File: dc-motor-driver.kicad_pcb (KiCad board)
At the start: 2 copper layers, 19.6 x 31.9 mm, 18 parts, among them J1 BAT, J2 Logic, J3 FL, J4 RL, J5 FR, J6 RR, J7 Power, Q1 IRF7303, Q2 IRF7303

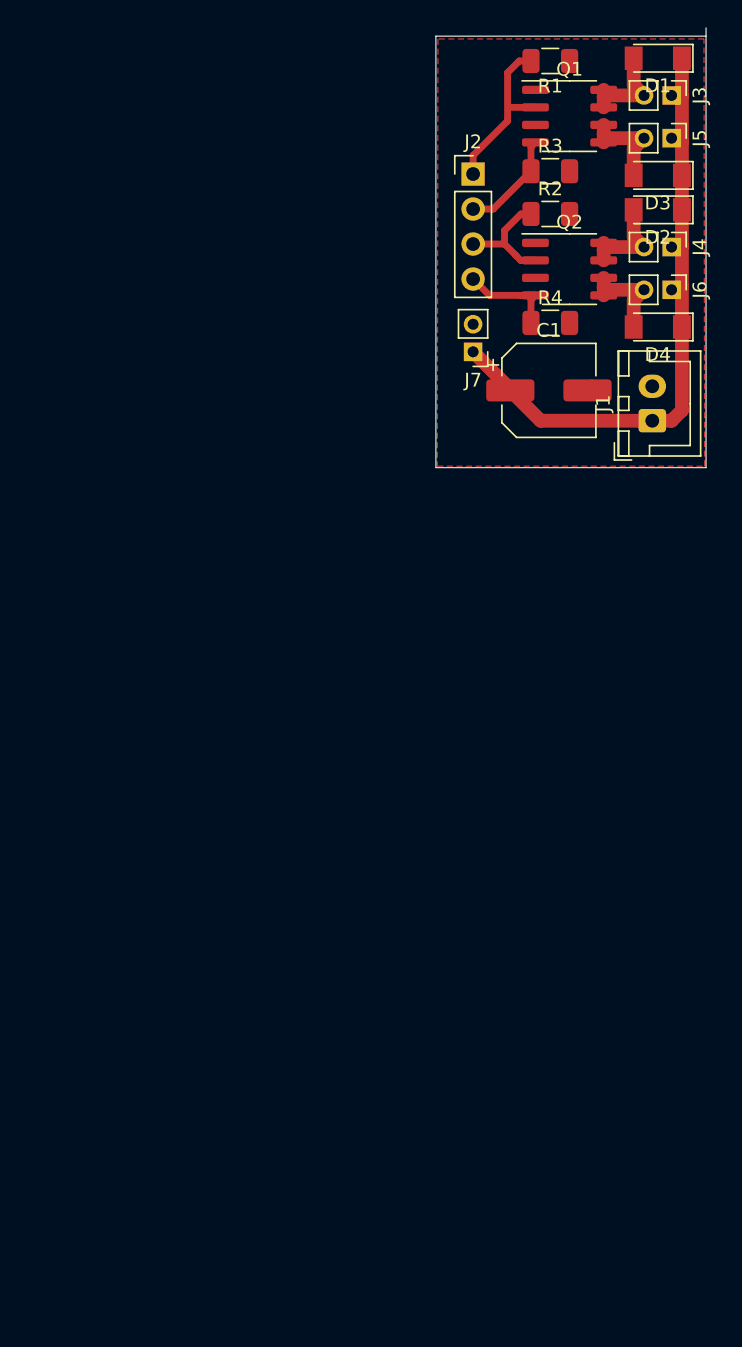
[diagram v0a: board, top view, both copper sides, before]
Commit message: Redesigned the board to work with TTGO T7 modules.
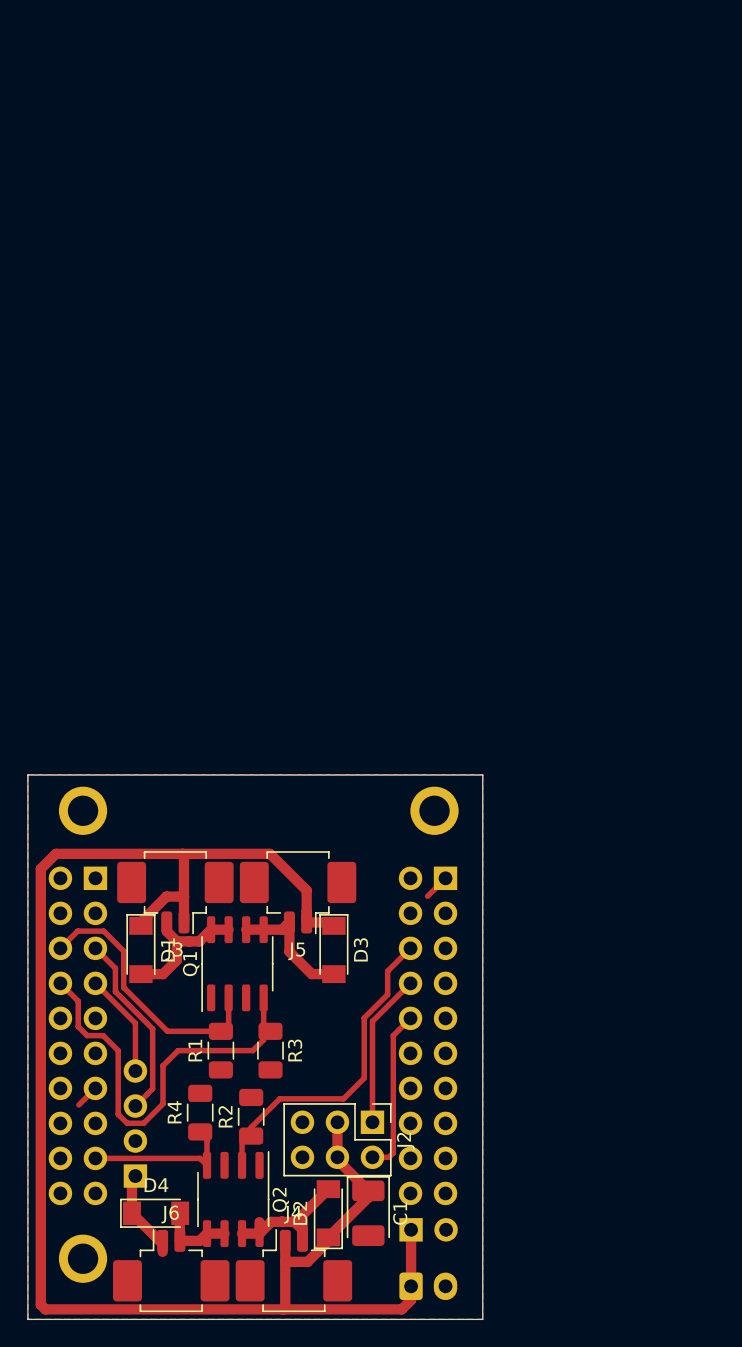
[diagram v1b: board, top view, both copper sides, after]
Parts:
- added ?: MountingHole_2.2mm_M2, MountingHole:MountingHole_2.2mm_M2, F.Cu at (83.0, 112.6)
- added ?: MountingHole_2.2mm_M2, MountingHole:MountingHole_2.2mm_M2, F.Cu at (83.0, 145.1)
- added ?: MountingHole_2.2mm_M2, MountingHole:MountingHole_2.2mm_M2, F.Cu at (108.5, 112.6)
- added J10: Right, Connector_PinHeader_2.54mm:PinHeader_2x10_P2.54mm_Vertical, B.Cu at (83.9, 117.5)
- added J8: MPU, Connector_PinHeader_2.54mm:PinHeader_1x04_P2.54mm_Vertical, B.Cu at (86.8, 139.1)
- added J9: Left, Connector_PinHeader_2.54mm:PinHeader_2x10_P2.54mm_Vertical, B.Cu at (109.3, 117.5)
- C1: value 2000uF -> C; footprint Capacitor_SMD:CP_Elec_6.3x5.9 -> Capacitor_Tantalum_SMD:CP_EIA-3528-21_Kemet-B_Pad1.50x2.35mm_HandSolder
- J1: moved to B.Cu
- J2: value Logic -> Conn_02x03_Odd_Even; footprint Connector_PinHeader_2.54mm:PinHeader_1x04_P2.54mm_Vertical -> Connector_PinHeader_2.54mm:PinHeader_2x03_P2.54mm_Vertical
- J3, J4, J5, J6: footprint Connector_PinHeader_2.00mm:PinHeader_1x02_P2.00mm_Vertical -> Connector_Molex:Molex_PicoBlade_53261-0271_1x02-1MP_P1.25mm_Horizontal
- J7: footprint Connector_PinHeader_2.00mm:PinHeader_1x02_P2.00mm_Vertical -> Connector_PinHeader_2.54mm:PinHeader_1x02_P2.54mm_Vertical; moved to B.Cu
- moved J6 80.1 mm to (89.4, 146.2), turned to 0 degrees
- moved J4 79.4 mm to (98.3, 146.2), turned to 0 degrees
- moved D2 76.6 mm to (100.8, 141.8), turned to 90 degrees
- moved R1 75.7 mm to (93.0, 130.0), turned to 90 degrees
- moved D1 74.8 mm to (87.2, 122.7), turned to 270 degrees
- moved D4 73.9 mm to (88.3, 141.8), turned to 0 degrees
- moved Q2 71.8 mm to (93.9, 140.8), turned to 270 degrees
- moved J2 69.2 mm to (104.0, 135.2), turned to 270 degrees
- moved R2 69.0 mm to (95.2, 134.8), turned to 90 degrees
- moved J3 67.9 mm to (89.7, 118.3), turned to 180 degrees
- moved R3 67.0 mm to (96.6, 130.0), turned to 270 degrees
- moved Q1 66.1 mm to (94.2, 123.7), turned to 90 degrees
- moved J1 65.2 mm to (106.8, 147.1), turned to 0 degrees
- moved J7 63.9 mm to (106.8, 143.0), turned to 270 degrees
- moved R4 62.7 mm to (91.5, 134.5), turned to 90 degrees
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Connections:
- J2 pad 1: /FL -> /ServoA
- J2 pad 2: /FR -> /ServoB
- J2 pad 3: /RL -> VCC
- J2 pad 4: /RR -> VCC
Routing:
- net VCC: track 46.4 -> 124.5 mm
- net /FR: track 8.02 -> 29.9 mm
- net /RL: track 8.42 -> 23.5 mm
- net /SCL: track 0.00 -> 13.7 mm
- net /ServoB: track 0.00 -> 12.6 mm
- net /ServoA: track 0.00 -> 11.2 mm
- net /FL: track 12.6 -> 20.7 mm
- net /SDA: track 0.00 -> 7.56 mm
- net /RR: track 8.22 -> 12.2 mm
- net Net-(D2-Pad2): track 7.30 -> 11.2 mm
- net GND: track 0.42 -> 3.54 mm
- net Net-(D1-Pad2): track 7.26 -> 10.2 mm
- net Net-(D3-Pad2): track 7.32 -> 9.84 mm
- net Net-(D4-Pad2): track 7.28 -> 5.68 mm
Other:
- board size 19.6 x 31.9 mm -> 33 x 39.5 mm

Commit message: Added a third servo and an LED.
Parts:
- removed the D4 at (88.3, 141.8)
- removed the J2 at (104.0, 135.2)
- removed the J3 at (89.7, 118.3)
- removed the J9 at (109.3, 117.5)
- added C1: 20uF, Capacitor_SMD:C_1206_3216Metric_Pad1.42x1.75mm_HandSolder, F.Cu at (89.2, 137.9)
- added D2: LL4148, Diode_SMD:D_MiniMELF, F.Cu at (98.5, 124.4)
- added D5: LL4148, Diode_SMD:D_MiniMELF, F.Cu at (88.3, 141.8)
- added J1: Conn_01x03, Connector_PinHeader_2.54mm:PinHeader_1x03_P2.54mm_Vertical, F.Cu at (103.6, 133.3)
- added J4: Conn_01x03, Connector_PinHeader_2.54mm:PinHeader_1x03_P2.54mm_Vertical, F.Cu at (103.6, 136.0)
- added J6: Left, Connector_PinHeader_2.54mm:PinHeader_2x10_P2.54mm_Vertical, B.Cu at (109.3, 117.5)
- added J7: Conn_01x03, Connector_PinHeader_2.54mm:PinHeader_1x03_P2.54mm_Vertical, F.Cu at (103.6, 138.7)
- added J8: FL, Connector_Molex:Molex_PicoBlade_53261-0271_1x02-1MP_P1.25mm_Horizontal, F.Cu at (89.7, 118.3)
- added R1: 10k, Resistor_SMD:R_1206_3216Metric, F.Cu at (104.6, 122.7)
- C2: renamed from C1; value C -> 20uF
- D3: value LL4148 -> LED; footprint Diode_SMD:D_MiniMELF -> LED_SMD:LED_1206_3216Metric_Pad1.42x1.75mm_HandSolder
- moved D3 6.21 mm to (104.6, 117.5)
- moved D1 3.11 mm to (89.8, 124.4), turned to 90 degrees
- moved D4 1.61 mm to (99.2, 141.6), turned to 180 degrees
- moved C2 0.60 mm to (103.7, 142.4)
- moved R4 0.40 mm to (94.8, 134.8)
- moved R2 0.10 mm to (93.1, 130.0)
- renumbered D2 to D4, J4 to J11, J6 to J12, J8 to J2, J1 to J3, J7 to J5, J5 to J9, R1 to R2, R2 to R4, R4 to R5
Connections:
- D3 pad 1: VCC -> GND
- J9 pad 2: Net-(D3-Pad2) -> Net-(D2-Pad2)
- Q1 pad 5: Net-(D3-Pad2) -> Net-(D2-Pad2)
- Q1 pad 6: Net-(D3-Pad2) -> Net-(D2-Pad2)
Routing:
- net VCC: track 124.5 -> 147.0 mm
- net /ServoC: track 0.00 -> 10.4 mm
- net /RL: track 23.5 -> 31.2 mm
- net Net-(D3-Pad2): track 9.84 -> 2.31 mm
- net Net-(D2-Pad2): track 0.00 -> 5.79 mm
- net /LED: track 0.00 -> 5.31 mm
- net Net-(D4-Pad2): track 11.2 -> 7.27 mm
- net /ServoB: track 12.6 -> 9.55 mm
- net GND: track 3.54 -> 6.01 mm
- net Net-(D1-Pad2): track 10.2 -> 7.98 mm
- net /ServoA: track 11.2 -> 9.39 mm

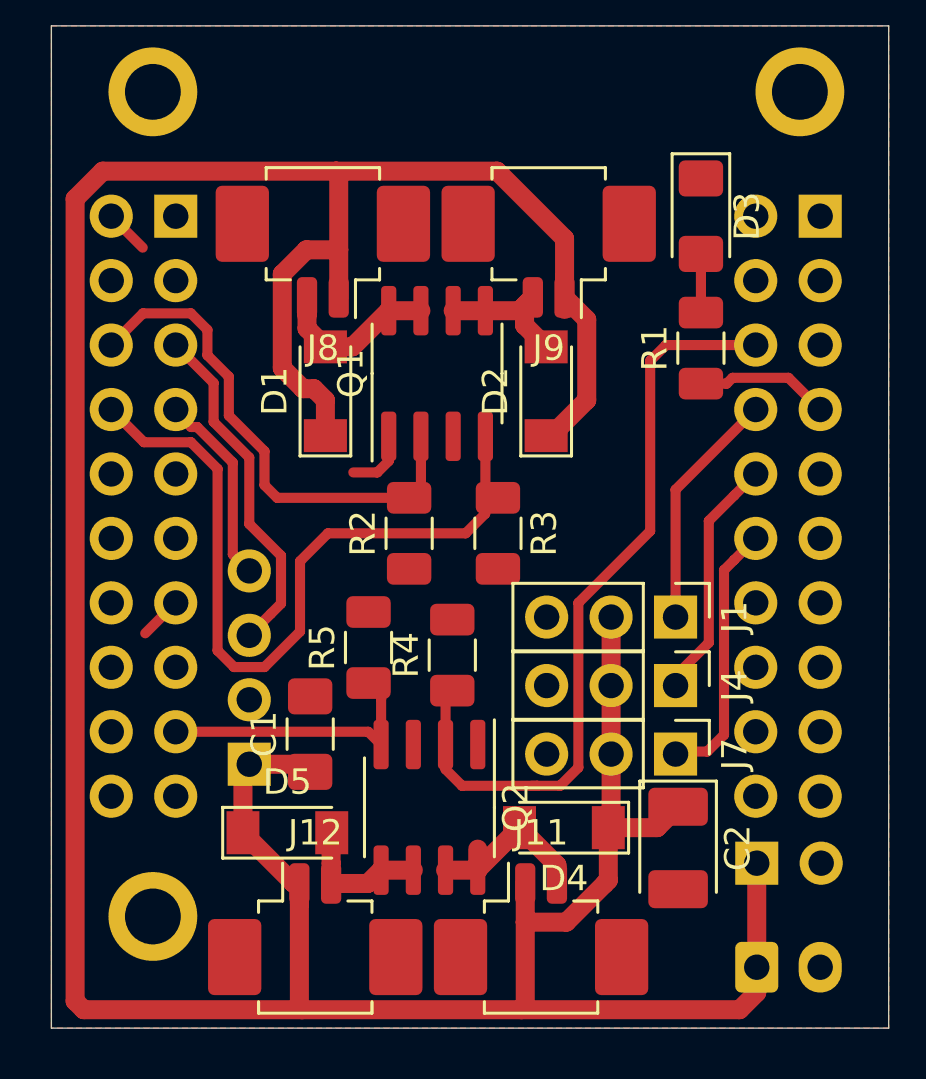
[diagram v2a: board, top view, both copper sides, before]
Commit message: Improved the ground plane.
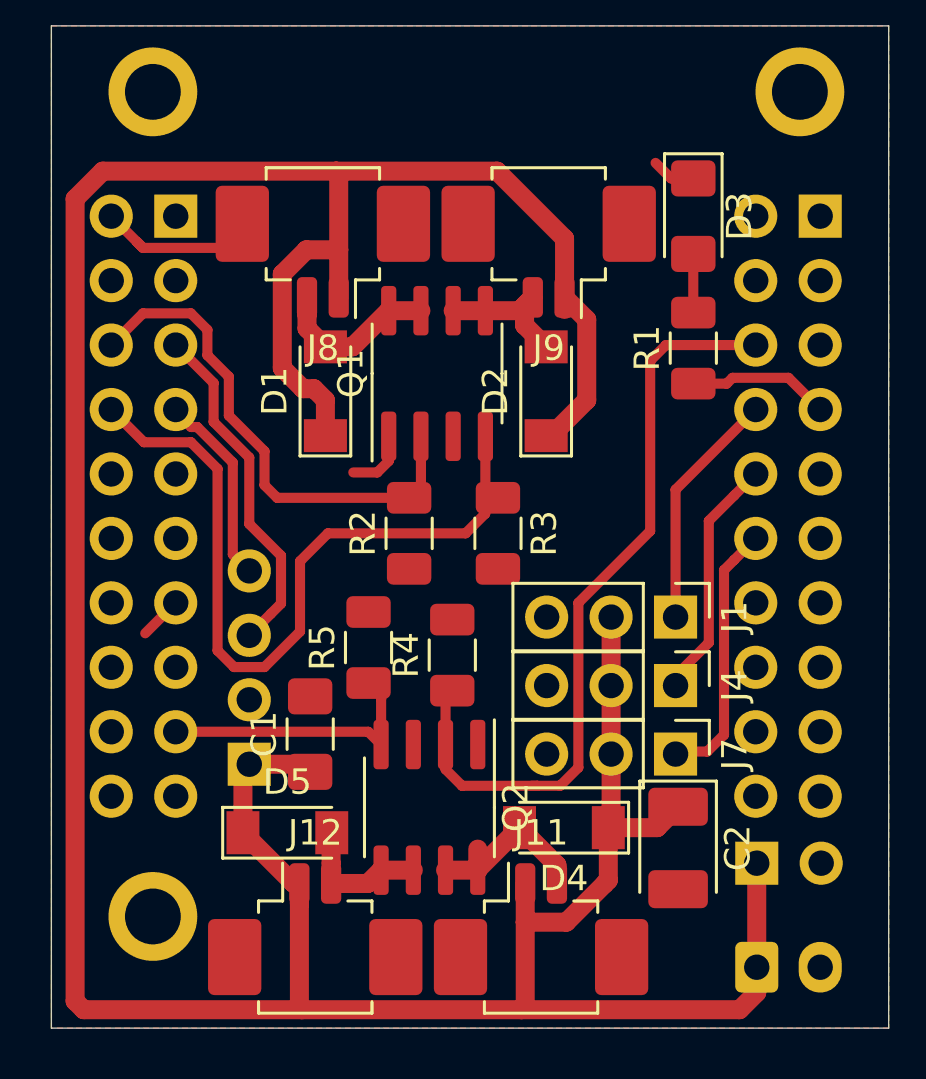
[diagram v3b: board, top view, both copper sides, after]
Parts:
- moved D3 0.30 mm to (104.3, 117.5)
- moved R1 0.30 mm to (104.3, 122.7)
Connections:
- J11 pad MP: (no net) -> GND
- J12 pad MP: (no net) -> GND
- J8 pad MP: (no net) -> GND
- J9 pad MP: (no net) -> GND
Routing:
- net GND: track 6.01 -> 12.4 mm
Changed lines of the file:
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@@
     (thickness 1.6)
     (drawings 4)
-    (tracks 159)
+    (tracks 165)
     (zones 0)
     (modules 29)
@@
     (mod_text_size 1 1)
     (mod_text_width 0.15)
-    (pad_size 3.5 3.5)
-    (pad_drill 2.2)
+    (pad_size 2.1 3)
+    (pad_drill 0)
     (pad_to_mask_clearance 0.051)
     (solder_mask_min_width 0.25)
@@
   )
   (module Resistor_SMD:R_1206_3216Metric (layer F.Cu)
-    (at 104.6 122.7 90)
+    (at 104.3 122.7 90)
     (descr "Resistor SMD 1206 (3216 Metric), square (rectangular) end terminal, IPC_7351 nominal, (Body size source: http://www.tortai-tech.com/upload/download/2011102023233369053.pdf), generated with kicad-footprint-generator")
     (tags resistor)
@@
   )
   (module LED_SMD:LED_1206_3216Metric_Pad1.42x1.75mm_HandSolder (layer F.Cu)
-    (at 104.6 117.5 270)
+    (at 104.3 117.5 270)
     (descr "LED SMD 1206 (3216 Metric), square (rectangular) end terminal, IPC_7351 nominal, (Body size source: http://www.tortai-tech.com/upload/download/2011102023233369053.pdf), generated with kicad-footprint-generator")
     (tags "LED handsolder")
@@
     (fp_line (start -2.235 -1.26) (end -2.235 -1.71) (layer F.SilkS) (width 0.12))
     (fp_line (start -2.125 -1.6) (end 2.125 -1.6) (layer F.Fab) (width 0.1))
-    (pad MP smd roundrect (at 3.175 0.5 180) (size 2.1 3) (layers F.Cu F.Paste F.Mask) (roundrect_rratio 0.119048))
+    (pad MP smd roundrect (at 3.175 0.5 180) (size 2.1 3) (layers F.Cu F.Paste F.Mask) (roundrect_rratio 0.119)
+      (net 2 GND))
     (pad MP smd roundrect (at -3.175 0.5 180) (size 2.1 3) (layers F.Cu F.Paste F.Mask) (roundrect_rratio 0.119048))
     (pad 2 smd roundrect (at 0.625 -2.4 180) (size 0.8 1.6) (layers F.Cu F.Paste F.Mask) (roundrect_rratio 0.25)
@@
     (fp_line (start -2.125 -1.6) (end 2.125 -1.6) (layer F.Fab) (width 0.1))
     (pad MP smd roundrect (at 3.175 0.5) (size 2.1 3) (layers F.Cu F.Paste F.Mask) (roundrect_rratio 0.119048))
-    (pad MP smd roundrect (at -3.175 0.5) (size 2.1 3) (layers F.Cu F.Paste F.Mask) (roundrect_rratio 0.119048))
+    (pad MP smd roundrect (at -3.175 0.5) (size 2.1 3) (layers F.Cu F.Paste F.Mask) (roundrect_rratio 0.119)
+      (net 2 GND))
     (pad 2 smd roundrect (at 0.625 -2.4) (size 0.8 1.6) (layers F.Cu F.Paste F.Mask) (roundrect_rratio 0.25)
       (net 29 "Net-(D5-Pad2)"))
@@
     (fp_line (start -2.125 -1.6) (end 2.125 -1.6) (layer F.Fab) (width 0.1))
     (pad MP smd roundrect (at 3.175 0.5 180) (size 2.1 3) (layers F.Cu F.Paste F.Mask) (roundrect_rratio 0.119048))
-    (pad MP smd roundrect (at -3.175 0.5 180) (size 2.1 3) (layers F.Cu F.Paste F.Mask) (roundrect_rratio 0.119048))
+    (pad MP smd roundrect (at -3.175 0.5 180) (size 2.1 3) (layers F.Cu F.Paste F.Mask) (roundrect_rratio 0.119)
+      (net 2 GND))
     (pad 2 smd roundrect (at 0.625 -2.4 180) (size 0.8 1.6) (layers F.Cu F.Paste F.Mask) (roundrect_rratio 0.25)
       (net 4 "Net-(D2-Pad2)"))
@@
     (fp_line (start -2.235 -1.26) (end -2.235 -1.71) (layer F.SilkS) (width 0.12))
     (fp_line (start -2.125 -1.6) (end 2.125 -1.6) (layer F.Fab) (width 0.1))
-    (pad MP smd roundrect (at 3.175 0.5) (size 2.1 3) (layers F.Cu F.Paste F.Mask) (roundrect_rratio 0.119048))
+    (pad MP smd roundrect (at 3.175 0.5) (size 2.1 3) (layers F.Cu F.Paste F.Mask) (roundrect_rratio 0.119)
+      (net 2 GND))
     (pad MP smd roundrect (at -3.175 0.5) (size 2.1 3) (layers F.Cu F.Paste F.Mask) (roundrect_rratio 0.119048))
     (pad 2 smd roundrect (at 0.625 -2.4) (size 0.8 1.6) (layers F.Cu F.Paste F.Mask) (roundrect_rratio 0.25)
@@
   (segment (start 92.295 126.175) (end 92.295 127.15) (width 0.4) (layer F.Cu) (net 2))
   (segment (start 91.845 127.6) (end 90.9 127.6) (width 0.4) (layer F.Cu) (net 2))
-  (segment (start 81.36 117.5) (end 82.6 118.74) (width 0.4) (layer F.Cu) (net 2))
   (segment (start 83.9 132.74) (end 82.7 133.94) (width 0.4) (layer F.Cu) (net 2))
+  (segment (start 103.425 116.0125) (end 102.8125 115.4) (width 0.4) (layer F.Cu) (net 2))
+  (segment (start 104.3 116.0125) (end 103.425 116.0125) (width 0.4) (layer F.Cu) (net 2))
+  (segment (start 82.610001 118.750001) (end 85.574999 118.750001) (width 0.4) (layer F.Cu) (net 2))
+  (segment (start 82.38 118.52) (end 82.610001 118.750001) (width 0.4) (layer F.Cu) (net 2))
+  (segment (start 82.38 118.52) (end 82.6 118.74) (width 0.4) (layer F.Cu) (net 2))
+  (segment (start 85.574999 118.750001) (end 86.525 117.8) (width 0.4) (layer F.Cu) (net 2))
+  (segment (start 81.36 117.5) (end 82.38 118.52) (width 0.4) (layer F.Cu) (net 2))
   (segment (start 92.295 121.225) (end 93.565 121.225) (width 0.75) (layer F.Cu) (net 3))
   (segment (start 89.075 120.7) (end 89.075 121.34603) (width 0.75) (layer F.Cu) (net 3))
@@
   (segment (start 97.65 121.8) (end 98.5 122.65) (width 0.75) (layer F.Cu) (net 4))
   (segment (start 97.65 121.025) (end 97.65 121.8) (width 0.75) (layer F.Cu) (net 4))
-  (segment (start 104.6 118.9875) (end 104.6 121.3) (width 0.4) (layer F.Cu) (net 5))
+  (segment (start 104.3 118.9875) (end 104.3 121.3) (width 0.4) (layer F.Cu) (net 5))
   (segment (start 95.805 143.245) (end 97.45 141.6) (width 0.75) (layer F.Cu) (net 6))
   (segment (start 95.805 143.275) (end 95.805 143.245) (width 0.75) (layer F.Cu) (net 6))
